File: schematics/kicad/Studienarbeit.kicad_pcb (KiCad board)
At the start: 2 copper layers, 41 parts, among them U1 ESP32-WROOM-32E, U2 PCM5102, U3 MCP6001-OT, U4 MCP6001-OT, U5 MCP6001, U6 TPA711

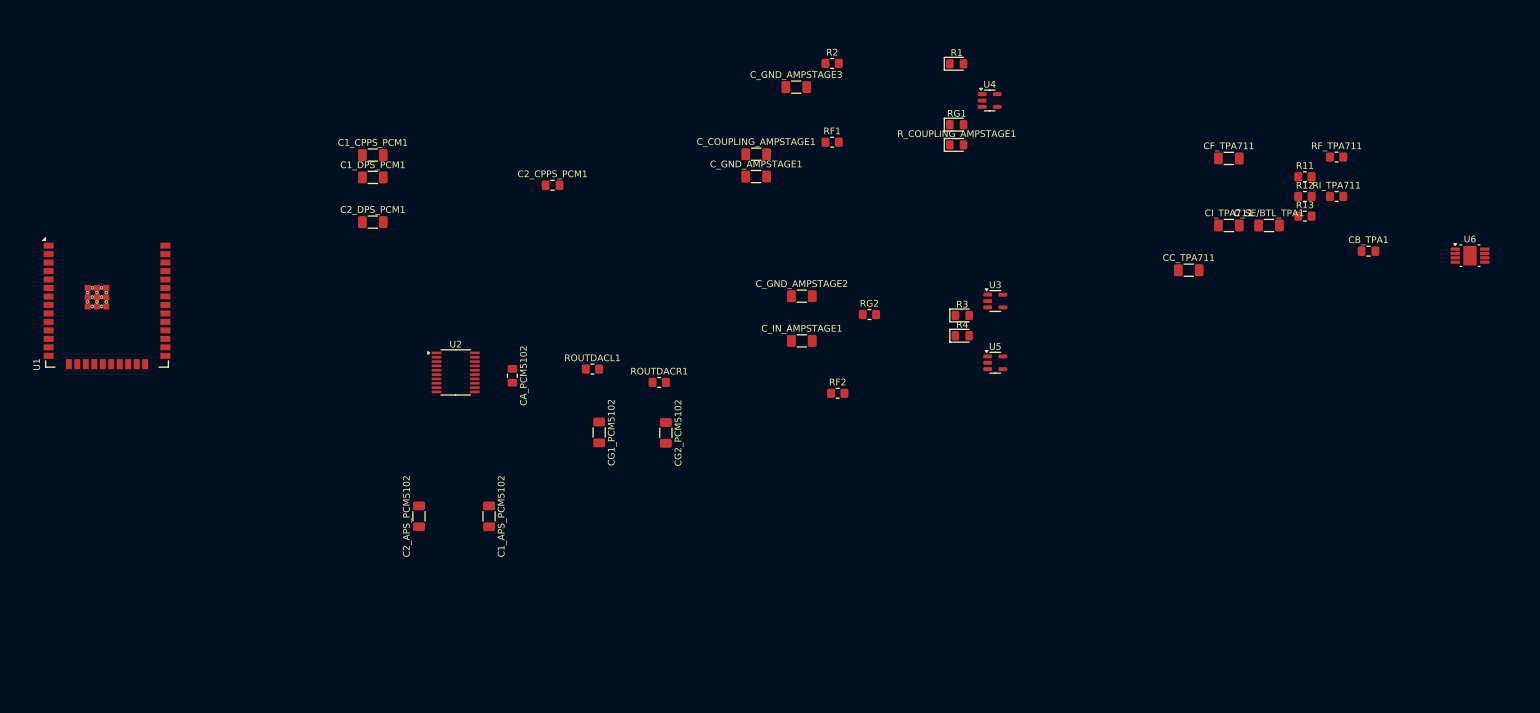
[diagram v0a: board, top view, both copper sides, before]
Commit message: KiCad: Added an LDO for stable supply voltage.
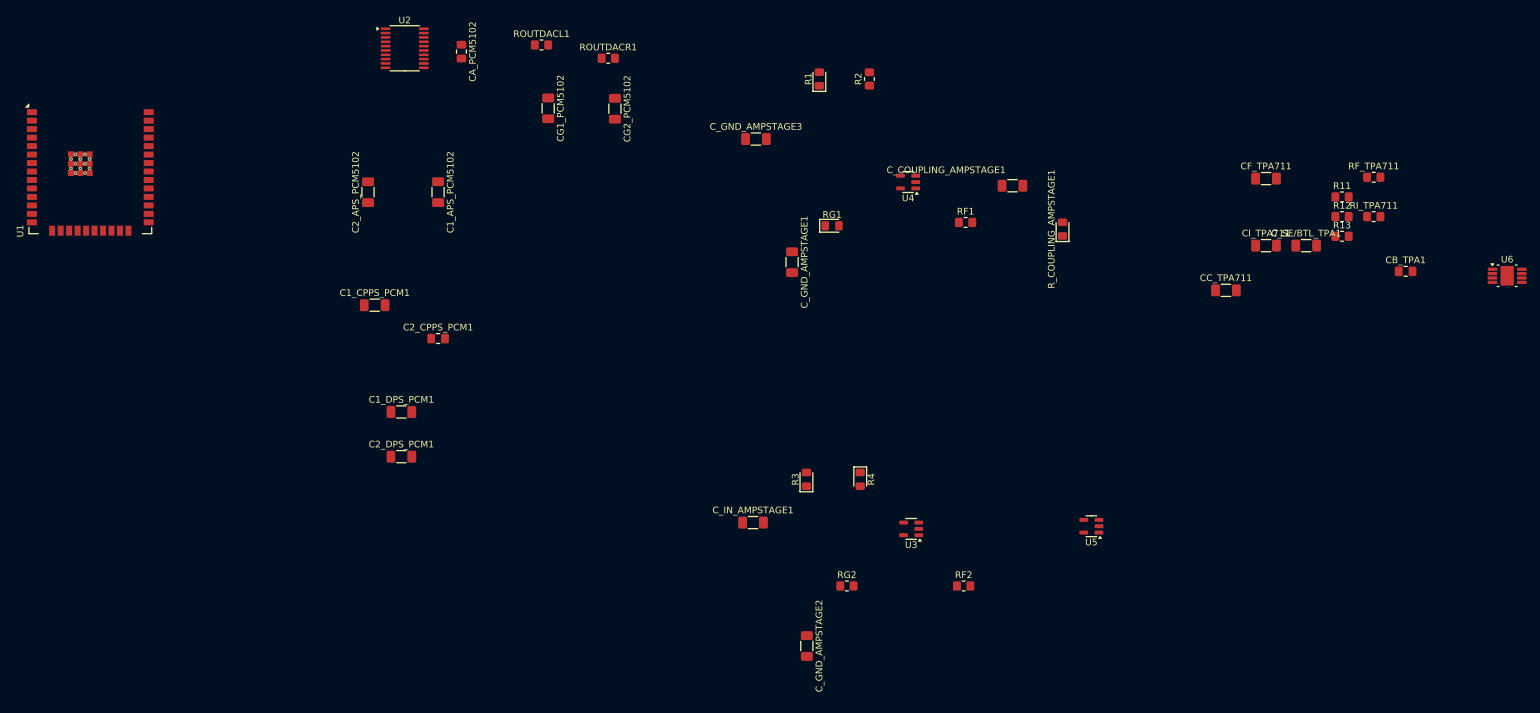
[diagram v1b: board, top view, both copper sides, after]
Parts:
- moved C_GND_AMPSTAGE2 52.4 mm to (159.1, 147.0), turned to -90 degrees
- moved C1_APS_PCM5102 49.2 mm to (103.9, 79.0)
- moved C2_APS_PCM5102 49.2 mm to (93.4, 79.0)
- moved CA_PCM5102 49.2 mm to (107.4, 57.9)
- moved CG1_PCM5102 49.2 mm to (120.4, 66.4)
- moved CG2_PCM5102 49.2 mm to (130.4, 66.5)
- moved ROUTDACL1 49.2 mm to (119.4, 56.9)
- moved ROUTDACR1 49.2 mm to (129.4, 58.9)
- moved U2 49.2 mm to (98.9, 57.4)
- moved RG2 40.8 mm to (165.1, 138.0)
- moved C_COUPLING_AMPSTAGE1 38.7 mm to (189.9, 78.0)
- moved U3 36.4 mm to (174.8, 129.4), turned to 180 degrees
- moved C2_DPS_PCM1 35.4 mm to (98.4, 118.6)
- moved C1_DPS_PCM1 35.4 mm to (98.4, 111.9)
- moved RF2 34.5 mm to (182.6, 138.0)
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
